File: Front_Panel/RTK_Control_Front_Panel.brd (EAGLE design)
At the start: 158.6 x 41 mm, 21 parts

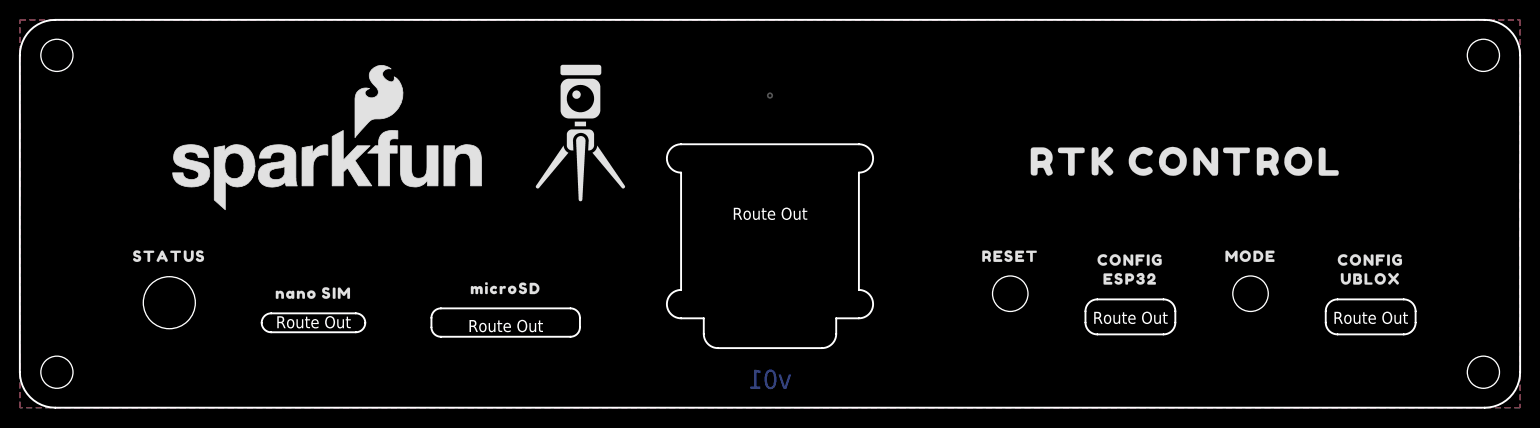
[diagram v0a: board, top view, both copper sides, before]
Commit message: Add 1.3" OLED
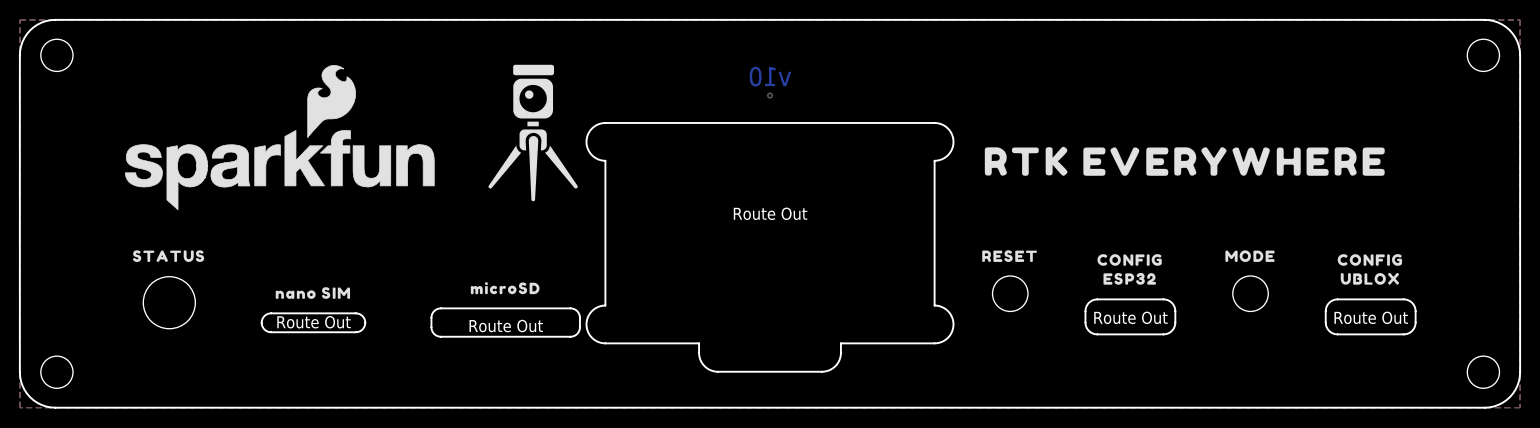
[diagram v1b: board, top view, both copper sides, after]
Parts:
- removed U$5: (no value), output:RTK_CONTROL0
- added U$1: (no value), output:RTK_EVERYWHERE0
- OLED: value OLED_14532 -> OLED_1.3_128X64; device SparkFun-Enclosure-Panel:OLED -> SparkFun-Enclosure-Panel:OLED-1.3-128X64
- moved LOGO1 5.00 mm to (-51.9, 17.1)
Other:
- board text added: "v10"
- board text removed: "v01"
